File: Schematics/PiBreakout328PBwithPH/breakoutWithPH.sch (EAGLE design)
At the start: 19 parts, among them J1 FEMALE 2x3, U2 ATMEGA328P_TQFP

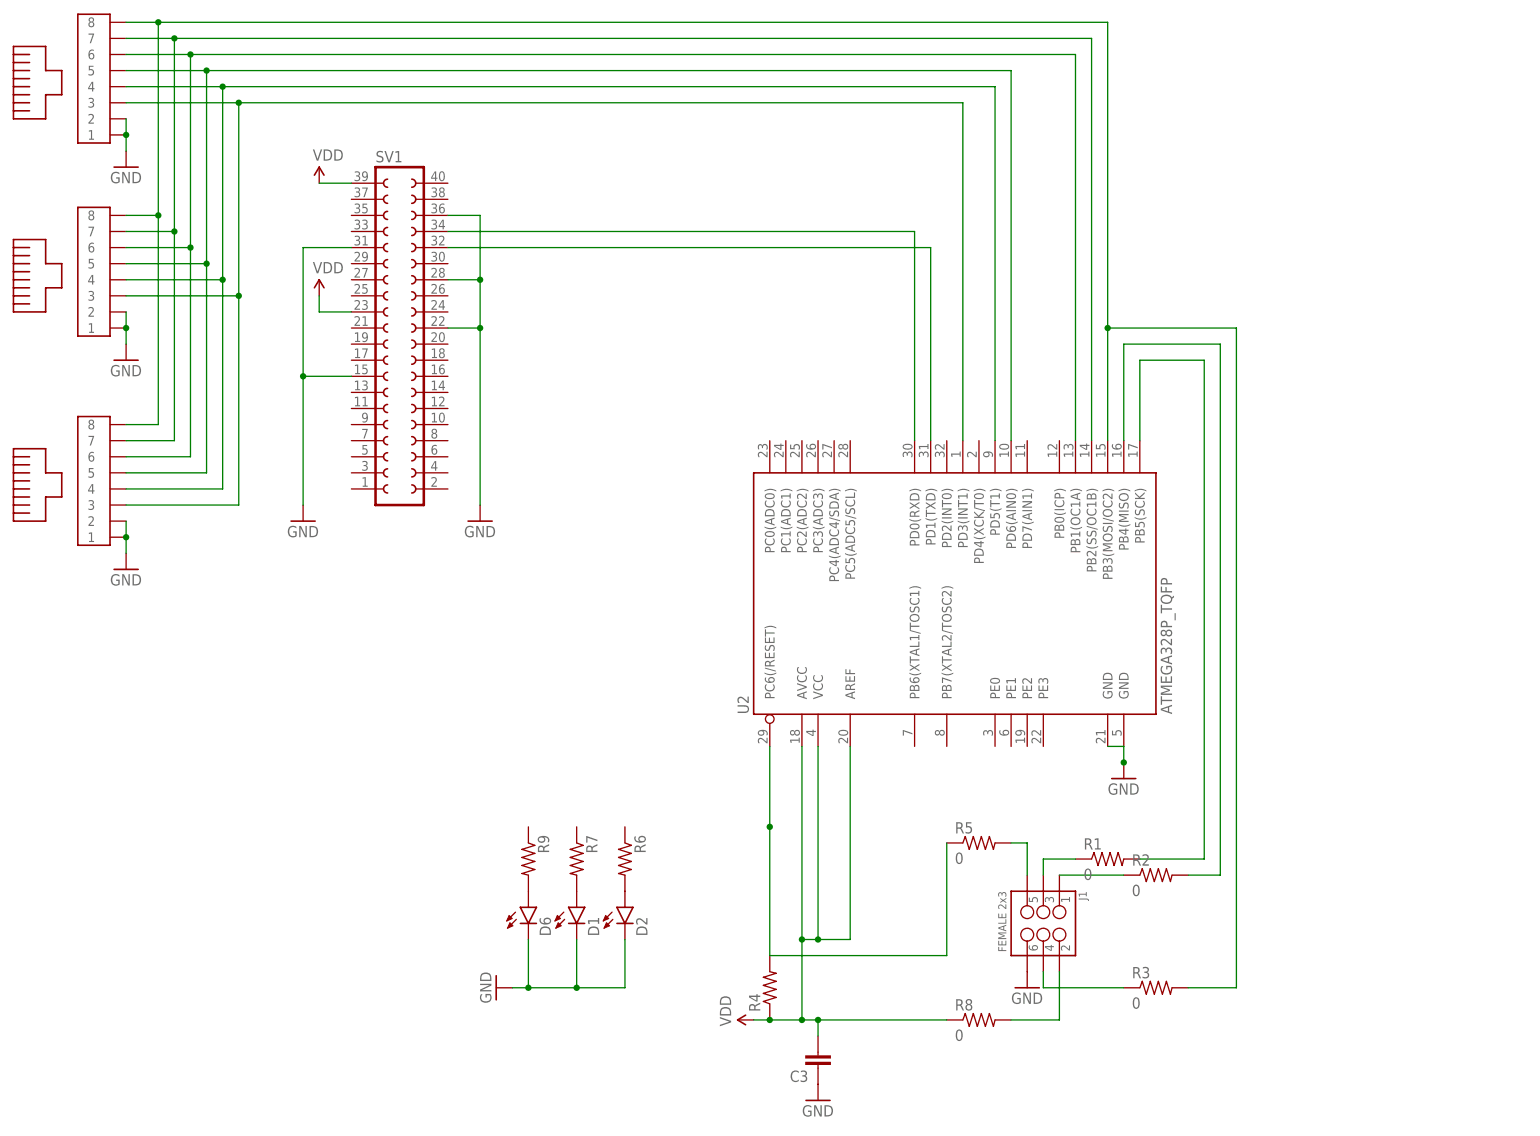
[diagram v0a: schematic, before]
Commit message: New breakout with PH, temp, and moisture sensor
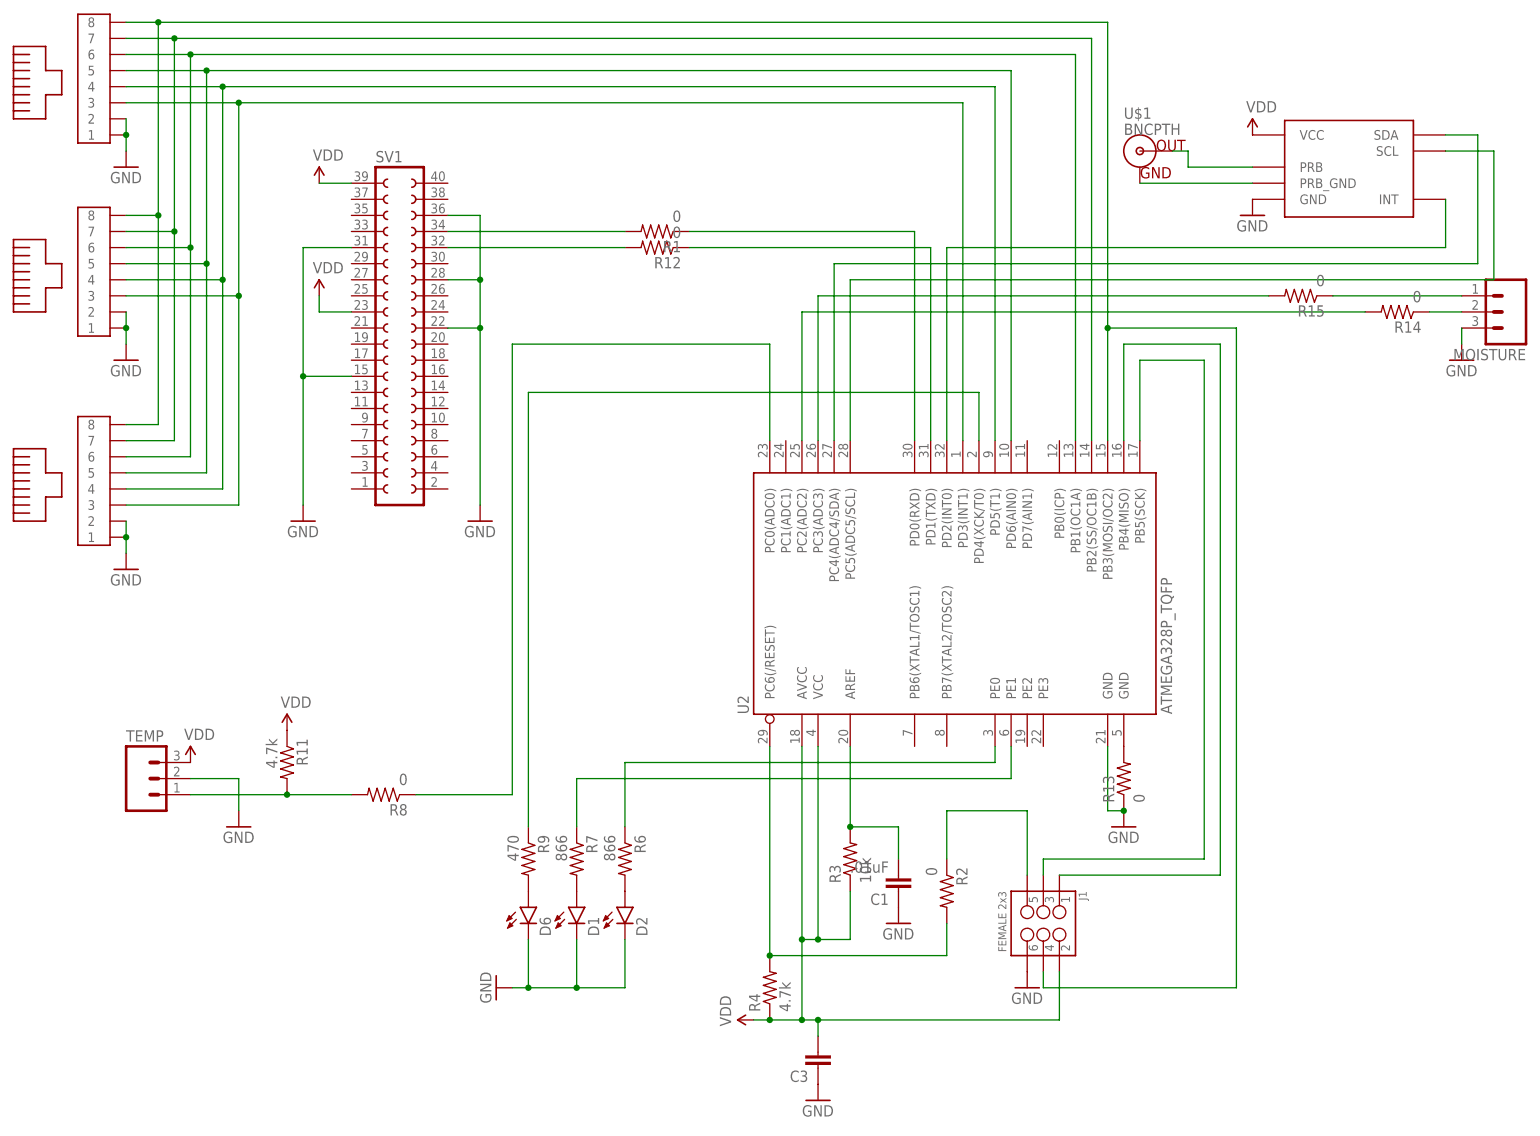
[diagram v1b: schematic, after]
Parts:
- removed R5: 0, SparkFun-Resistors:RESISTOR1206
- added C1: .01uF, SparkFun-Capacitors:CAP1206
- added MOISTURE, TEMP: (no value), SparkFun-Connectors:M03LOCK_LONGPADS
- added R11: 4.7k, SparkFun-Resistors:RESISTOR1206
- added R12, R13, R14, R15: 0, SparkFun-Resistors:RESISTOR1206
- added U$1: BNCPTH, SparkFun-Connectors:BNCPTH
- added U1: PH_SMD, custom-mlane:PH_SMD
- R3: value 0 -> 10k
- R4: value (none) -> 4.7k
- R6, R7: value (none) -> 866
- R9: value (none) -> 470
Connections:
- new net N$21: C1.2, R3.2, U2.AREF
- new net N$23: R8.1, U2.PC0(ADC0)
- new net N$24: R11.2, R8.2, TEMP.1
- new net N$25: U1.SCL, U2.PC5(ADC5/SCL)
- new net N$26: U1.SDA, U2.PC4(ADC4/SDA)
- new net N$27: R12.2, SV1.32
- new net N$28: R13.2, U2.GND@5
- new net N$29: U$1.OUT, U1.PRB
- new net N$30: R15.2, U2.PC3(ADC3)
- new net N$31: R14.2, U2.PC2(ADC2)
- new net N$32: MOISTURE.2, R14.1
- new net N$33: MOISTURE.1, R15.1
- new net N$9: R9.1, U2.PD4(XCK/T0)
- new net PRB_GND: U$1.GND, U1.PRB_GND
- net GND: now also C1.1, MOISTURE.3, R13.1, TEMP.2, U1.GND; no longer U2.GND@5
- net N$1: now also R12.1; no longer SV1.32
- net N$10: now also R1.1; no longer SV1.34
- net N$11: now also U2.PB5(SCK); no longer R1.1
- net N$14: now also U2.PB4(MISO); no longer R2.1
- net N$15: now also R6.1, U2.PE0; no longer J1.2, R8.2
- net N$16: now also U1.INT, U2.PD2(INT0); no longer R2.2, U2.PB4(MISO)
- net N$17: now also R7.1, U2.PE1; no longer R1.2, U2.PB5(SCK)
- net N$19: now also R1.2, SV1.34; no longer J1.4, R3.1
- net N$2: now also J1.5, R2.1; no longer R4.2, R5.1, U2.PC6(/RESET)
- net N$5: now also J1.4; no longer R3.2
- net N$8: now also R2.2, R4.2, U2.PC6(/RESET); no longer J1.5, R5.2
- net VDD: now also J1.2, R11.1, R3.1, TEMP.3, U1.VCC; no longer R8.1, U2.AREF
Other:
- moved on the sheet: R1, R2, R3, R8

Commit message: Temperature and PH firmware
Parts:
- added R5: 4.7k, SparkFun-Resistors:RESISTOR1206
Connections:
- net N$25: now also R5.2
- net N$26: now also R4.2
- net N$8: no longer R4.2
- net VDD: now also R5.1
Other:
- moved on the sheet: R4
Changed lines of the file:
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@@
 <part name="U2" library="custom-mlane" deviceset="ATMEGA328P_TQFP" device=""/>
 <part name="SUPPLY2" library="SparkFun-Aesthetics" deviceset="VDD" device=""/>
-<part name="R4" library="SparkFun-Resistors" deviceset="RESISTOR" device="1206" value="4.7k"/>
 <part name="J1" library="SparkFun-Connectors" deviceset="M03X2" device="FEMALE" value="FEMALE 2x3"/>
 <part name="GND5" library="SparkFun-Aesthetics" deviceset="GND" device=""/>
@@
 <part name="GND4" library="SparkFun-Aesthetics" deviceset="GND" device=""/>
 <part name="R3" library="SparkFun-Resistors" deviceset="RESISTOR" device="1206" value="10k"/>
+<part name="R4" library="SparkFun-Resistors" deviceset="RESISTOR" device="1206" value="4.7k"/>
+<part name="SUPPLY5" library="SparkFun-Aesthetics" deviceset="VDD" device=""/>
+<part name="R5" library="SparkFun-Resistors" deviceset="RESISTOR" device="1206" value="4.7k"/>
+<part name="SUPPLY6" library="SparkFun-Aesthetics" deviceset="VDD" device=""/>
 </parts>
 <sheets>
@@
 <instance part="U2" gate="U$1" x="20.32" y="12.7" rot="R90"/>
 <instance part="SUPPLY2" gate="VDD" x="-12.7" y="-55.88" rot="R90"/>
-<instance part="R4" gate="G$1" x="-10.16" y="-50.8" rot="R90"/>
 <instance part="J1" gate="G$1" x="33.02" y="-40.64" rot="R270"/>
 <instance part="GND5" gate="1" x="30.48" y="-50.8"/>
@@
 <instance part="GND4" gate="1" x="10.16" y="-40.64"/>
 <instance part="R3" gate="G$1" x="2.54" y="-30.48" rot="R90"/>
+<instance part="R4" gate="G$1" x="101.6" y="88.9" rot="R270"/>
+<instance part="SUPPLY5" gate="VDD" x="101.6" y="93.98"/>
+<instance part="R5" gate="G$1" x="104.14" y="86.36" rot="R270"/>
+<instance part="SUPPLY6" gate="VDD" x="104.14" y="91.44"/>
 </instances>
 <busses>
@@
 <segment>
 <pinref part="SUPPLY2" gate="VDD" pin="VDD"/>
-<wire x1="-10.16" y1="-55.88" x2="-12.7" y2="-55.88" width="0.1524" layer="91"/>
-<pinref part="R4" gate="G$1" pin="1"/>
-<junction x="-10.16" y="-55.88"/>
 <pinref part="U2" gate="U$1" pin="VCC@4"/>
 <wire x1="-2.54" y1="-12.7" x2="-2.54" y2="-43.18" width="0.1524" layer="91"/>
@@
 <junction x="-5.08" y="-43.18"/>
 <wire x1="-5.08" y1="-43.18" x2="-5.08" y2="-55.88" width="0.1524" layer="91"/>
-<wire x1="-5.08" y1="-55.88" x2="-10.16" y2="-55.88" width="0.1524" layer="91"/>
+<wire x1="-5.08" y1="-55.88" x2="-12.7" y2="-55.88" width="0.1524" layer="91"/>
 <junction x="-5.08" y="-55.88"/>
 <pinref part="C3" gate="G$1" pin="2"/>
@@
 <pinref part="SUPPLY4" gate="VDD" pin="VDD"/>
 <pinref part="U1" gate="U1" pin="VCC"/>
+</segment>
+<segment>
+<pinref part="R4" gate="G$1" pin="1"/>
+<pinref part="SUPPLY5" gate="VDD" pin="VDD"/>
+</segment>
+<segment>
+<pinref part="R5" gate="G$1" pin="1"/>
+<pinref part="SUPPLY6" gate="VDD" pin="VDD"/>
 </segment>
 </net>
@@
 <pinref part="U2" gate="U$1" pin="PC6(/RESET)"/>
 <wire x1="-10.16" y1="-12.7" x2="-10.16" y2="-45.72" width="0.1524" layer="91"/>
-<pinref part="R4" gate="G$1" pin="2"/>
 <wire x1="17.78" y1="-45.72" x2="-10.16" y2="-45.72" width="0.1524" layer="91"/>
-<junction x="-10.16" y="-45.72"/>
 <pinref part="R2" gate="G$1" pin="2"/>
 <wire x1="17.78" y1="-40.64" x2="17.78" y2="-45.72" width="0.1524" layer="91"/>
@@
 <pinref part="U2" gate="U$1" pin="PC5(ADC5/SCL)"/>
 <wire x1="2.54" y1="35.56" x2="2.54" y2="60.96" width="0.1524" layer="91"/>
+<pinref part="R5" gate="G$1" pin="2"/>
+<junction x="104.14" y="81.28"/>
 </segment>
 </net>
@@
 <pinref part="U2" gate="U$1" pin="PC4(ADC4/SDA)"/>
 <wire x1="0" y1="35.56" x2="0" y2="63.5" width="0.1524" layer="91"/>
-</segment>
-</net>
+<pinref part="R4" gate="G$1" pin="2"/>
+<junction x="101.6" y="83.82"/>
+</segment>
+</net>
